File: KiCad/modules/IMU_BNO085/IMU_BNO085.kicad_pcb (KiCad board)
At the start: 2 copper layers, 26.8 x 22.5 mm, 7 parts, among them J1 Conn_01x01_Pin, J2 Conn_01x01_Pin, J3 Conn_01x01_Pin, J4 Conn_01x01_Pin, U1 BNO055

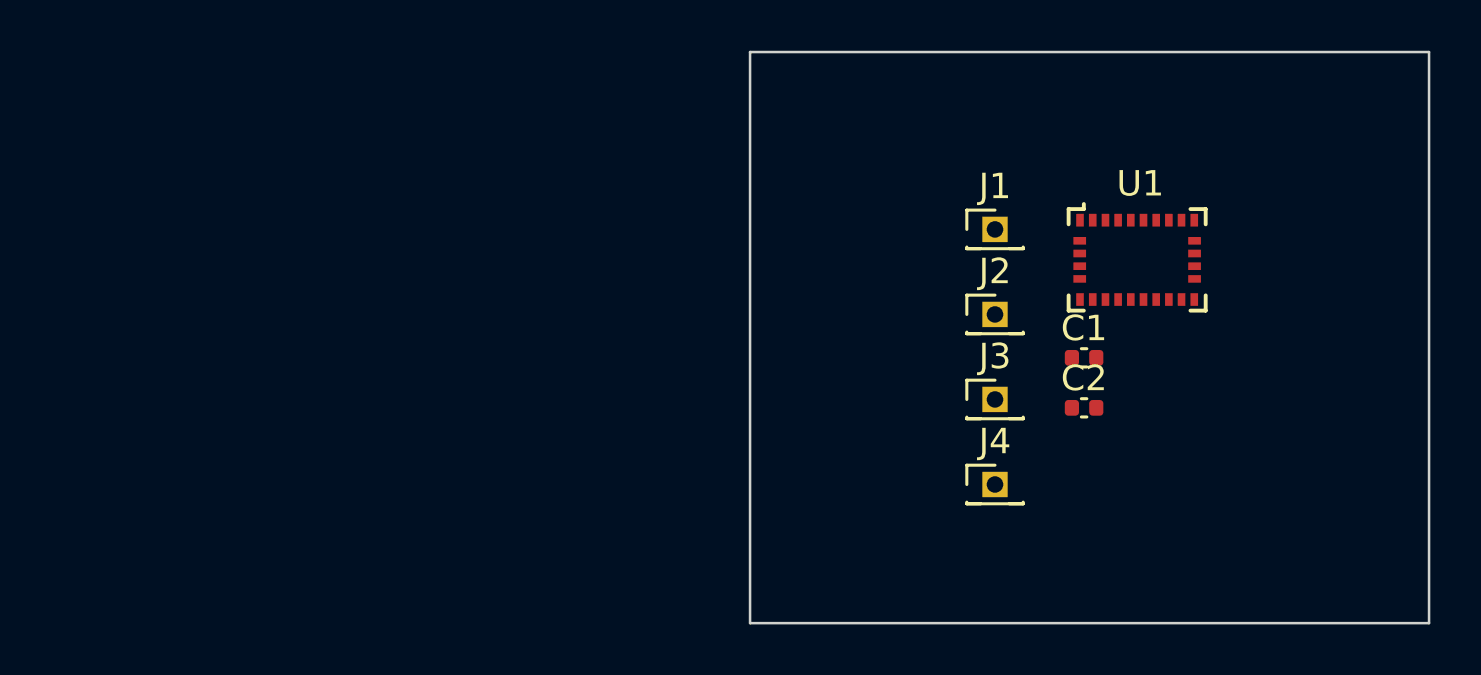
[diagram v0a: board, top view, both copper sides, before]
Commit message: finished ads93,commod,drypad,flexpad,jackconn,imubno + plot and render
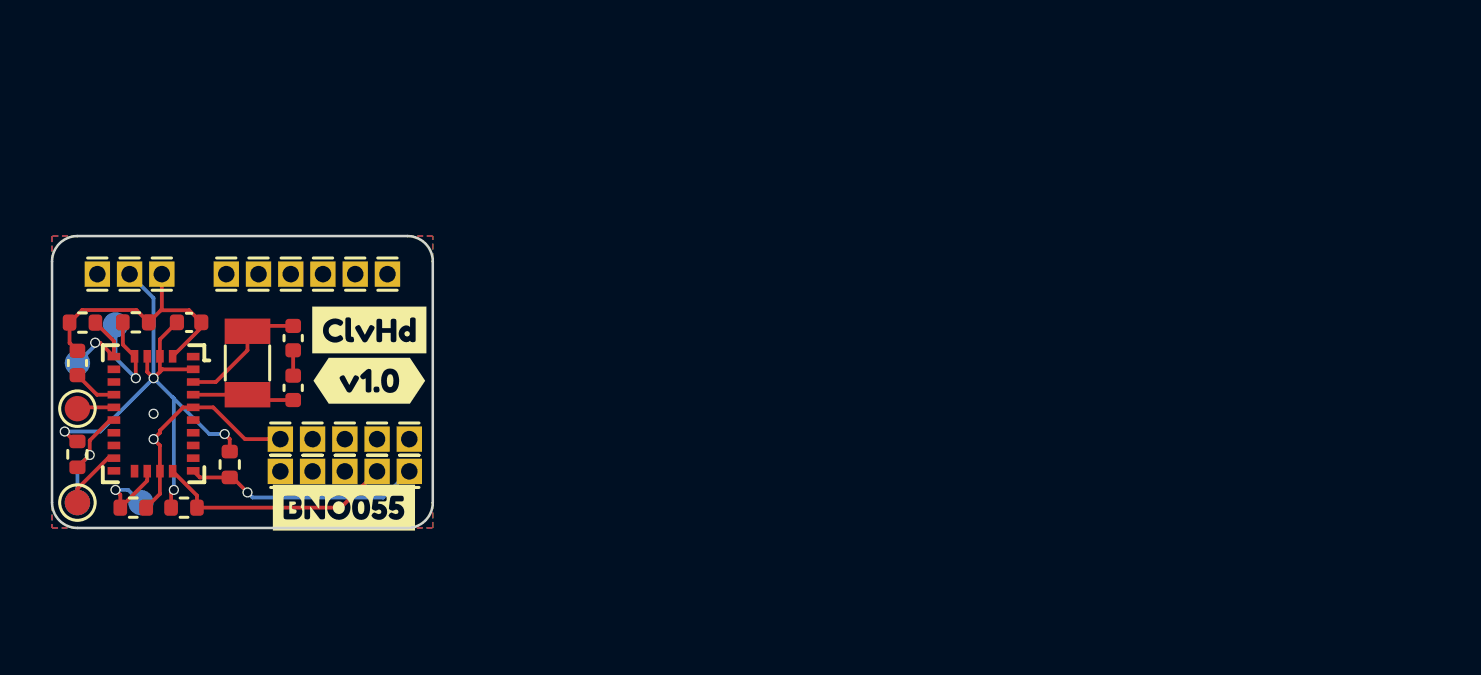
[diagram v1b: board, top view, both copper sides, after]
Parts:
- added C3: 22pF, Capacitor_SMD:C_0402_1005Metric, F.Cu at (119.5, 98.0)
- added C4: 22pF, Capacitor_SMD:C_0402_1005Metric, F.Cu at (119.5, 100.0)
- added J10: Conn_01x01_Pin, Connector_PinHeader_1.27mm:PinHeader_1x01_P1.27mm_Vertical, F.Cu at (123.2, 95.5)
- added J11: Conn_01x01_Pin, Connector_PinHeader_1.27mm:PinHeader_1x01_P1.27mm_Vertical, F.Cu at (119.0, 103.3)
- added J12: Conn_01x01_Pin, Connector_PinHeader_1.27mm:PinHeader_1x01_P1.27mm_Vertical, F.Cu at (120.3, 103.3)
- added J13: Conn_01x01_Pin, Connector_PinHeader_1.27mm:PinHeader_1x01_P1.27mm_Vertical, F.Cu at (120.7, 95.5)
- added J14: Conn_01x01_Pin, Connector_PinHeader_1.27mm:PinHeader_1x01_P1.27mm_Vertical, F.Cu at (121.9, 95.5)
- added J15: Conn_01x01_Pin, Connector_PinHeader_1.27mm:PinHeader_1x01_P1.27mm_Vertical, F.Cu at (111.8, 95.5)
- added J16: Conn_01x01_Pin, Connector_PinHeader_1.27mm:PinHeader_1x01_P1.27mm_Vertical, F.Cu at (116.9, 95.5)
- added J17: Conn_01x01_Pin, Connector_PinHeader_1.27mm:PinHeader_1x01_P1.27mm_Vertical, F.Cu at (118.1, 95.5)
- added J18: Conn_01x01_Pin, Connector_PinHeader_1.27mm:PinHeader_1x01_P1.27mm_Vertical, F.Cu at (119.4, 95.5)
- added J19: Conn_01x01_Pin, Connector_PinHeader_1.27mm:PinHeader_1x01_P1.27mm_Vertical, F.Cu at (119.0, 102.0)
- added J5: Conn_01x01_Pin, Connector_PinHeader_1.27mm:PinHeader_1x01_P1.27mm_Vertical, F.Cu at (120.3, 102.0)
- added J6: Conn_01x01_Pin, Connector_PinHeader_1.27mm:PinHeader_1x01_P1.27mm_Vertical, F.Cu at (121.5, 102.0)
- added J7: Conn_01x01_Pin, Connector_PinHeader_1.27mm:PinHeader_1x01_P1.27mm_Vertical, F.Cu at (122.8, 102.0)
- added J8: Conn_01x01_Pin, Connector_PinHeader_1.27mm:PinHeader_1x01_P1.27mm_Vertical, F.Cu at (124.1, 102.0)
- added J9: Conn_01x01_Pin, Connector_PinHeader_1.27mm:PinHeader_1x01_P1.27mm_Vertical, F.Cu at (121.5, 103.3)
- added R1: 10k, Resistor_SMD:R_0402_1005Metric, F.Cu at (113.2, 104.7)
- added R2: 10k, Resistor_SMD:R_0402_1005Metric, F.Cu at (111.2, 97.4)
- added R3: 10k, Resistor_SMD:R_0402_1005Metric, F.Cu at (113.3, 97.4)
- added R4: 10k, Resistor_SMD:R_0402_1005Metric, F.Cu at (117.0, 103.0)
- added R5: 10k, Resistor_SMD:R_0402_1005Metric, F.Cu at (115.2, 104.7)
- added R6: 10k, Resistor_SMD:R_0402_1005Metric, F.Cu at (111.0, 102.6)
- added TP1: TestPoint, 00_Custom:TestPoint_Pad_D1.0mm, F.Cu at (111.0, 100.8)
- added TP2: TestPoint, 00_Custom:TestPoint_Pad_D1.0mm, F.Cu at (111.0, 104.5)
- added TP3: TestPoint, 00_Custom:TestPoint_Pad_D1.0mm, B.Cu at (111.0, 99.0)
- added TP4: TestPoint, 00_Custom:TestPoint_Pad_D1.0mm, B.Cu at (112.5, 97.5)
- added TP5: TestPoint, 00_Custom:TestPoint_Pad_D1.0mm, B.Cu at (113.5, 104.5)
- added TP6: TestPoint, 00_Custom:TestPoint_Pad_D1.0mm, B.Cu at (111.0, 104.5)
- added Y1: Crystal, Crystal:Crystal_SMD_3215-2Pin_3.2x1.5mm, F.Cu at (117.7, 99.0)
- added kibuzzard-65916A49: G***, kibuzzard-65916A49, F.Cu at (121.5, 104.7)
- added kibuzzard-65916AA3: G***, kibuzzard-65916AA3, F.Cu at (122.5, 97.7)
- added kibuzzard-65916B62: G***, kibuzzard-65916B62, B.Cu at (117.5, 99.1)
- added kibuzzard-65916B8F: G***, kibuzzard-65916B8F, F.Cu at (122.5, 99.7)
- C1, C2: value 4.7uF -> 0.1uF
- U1: value BNO055 -> bno055
- moved C2 39.7 mm to (111.0, 99.0), turned to 90 degrees
- moved U1 39.2 mm to (114.0, 101.0), turned to -90 degrees
- moved C1 35.3 mm to (115.4, 97.4), turned to 180 degrees
- moved J1 34.1 mm to (113.1, 95.5)
- moved J4 33.9 mm to (114.3, 95.5)
- moved J3 24.5 mm to (122.8, 103.3)
- moved J2 23.9 mm to (124.1, 103.3)
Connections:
- C1 pad 1: unconnected-(C1-Pad1) -> GND
- C1 pad 2: unconnected-(C1-Pad2) -> +3.3V
- C2 pad 1: unconnected-(C2-Pad1) -> /CAP
- C2 pad 2: unconnected-(C2-Pad2) -> GND
- J1 pad 1: unconnected-(J1-Pin_1-Pad1) -> +3.3V
- J2 pad 1: unconnected-(J2-Pin_1-Pad1) -> /SDA
- J3 pad 1: unconnected-(J3-Pin_1-Pad1) -> /SCL
- J4 pad 1: unconnected-(J4-Pin_1-Pad1) -> GND
- U1 pad 10: unconnected-(U1-BL_IND-Pad10) -> /BL_IND
- U1 pad 11: unconnected-(U1-RESET-Pad11) -> /nRESET
- U1 pad 14: unconnected-(U1-INT-Pad14) -> /INT
- U1 pad 17: unconnected-(U1-COM3-Pad17) -> /I2C_ADD
- U1 pad 18: unconnected-(U1-COM2-Pad18) -> GND
- U1 pad 19: unconnected-(U1-COM1-Pad19) -> /SCL
- U1 pad 2: unconnected-(U1-GND-Pad2) -> GND
- U1 pad 20: unconnected-(U1-COM0-Pad20) -> /SDA
- U1 pad 25: unconnected-(U1-GNDIO-Pad25) -> GND
- U1 pad 26: unconnected-(U1-XOUT32-Pad26) -> /X_OUT
- U1 pad 27: unconnected-(U1-XIN32-Pad27) -> /X_IN
- U1 pad 28: unconnected-(U1-VDDIO-Pad28) -> +3.3V
- U1 pad 3: unconnected-(U1-VDD-Pad3) -> +3.3V
- U1 pad 4: unconnected-(U1-BOOT_LOAD-Pad4) -> +3.3V
- U1 pad 5: unconnected-(U1-PS1-Pad5) -> /PS1
- U1 pad 6: unconnected-(U1-PS0-Pad6) -> /PS0
- U1 pad 9: unconnected-(U1-CAP-Pad9) -> /CAP
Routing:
- net +3.3V: track 0.00 -> 23.3 mm, vias 0 -> 4
- net GND: track 0.00 -> 20.6 mm, vias 0 -> 2
- net /SCL: track 0.00 -> 9.52 mm
- net /SDA: track 0.00 -> 9.37 mm, vias 0 -> 1
- net /X_IN: track 0.00 -> 5.29 mm
- net /PS1: track 0.00 -> 4.84 mm, vias 0 -> 1
- net /nRESET: track 0.00 -> 4.62 mm, vias 0 -> 1
- net /X_OUT: track 0.00 -> 4.02 mm
- net /I2C_ADD: track 0.00 -> 3.86 mm, vias 0 -> 1
- net /PS0: track 0.00 -> 3.70 mm, vias 0 -> 1
- net /INT: track 0.00 -> 2.48 mm
- net /CAP: track 0.00 -> 1.76 mm
- net /BL_IND: track 0.00 -> 1.46 mm
- added copper zone on B.Cu, net GND
- added copper zone on F.Cu, net GND
- added copper zone on In1.Cu, net GND
- added copper zone on In2.Cu, net GND
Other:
- board size 26.8 x 22.5 mm -> 15 x 11.5 mm
- copper layers 2 -> 4
- board text added: "i2c_add"
- board text added: "ps0"
- board text added: "ps1"
- board text added: "reset"
